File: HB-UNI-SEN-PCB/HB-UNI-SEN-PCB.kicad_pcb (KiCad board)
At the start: 2 copper layers, 44.4 x 30.5 mm, 18 parts, among them J0 BATT, J1 I2C_1, J2 I2C_2, J3 A0, J4 A1, J5 A2, J6 A3, J7 PROG, SW1 CONFIG_BUTTON, U1 ArduinoProMini, U2 CC1101

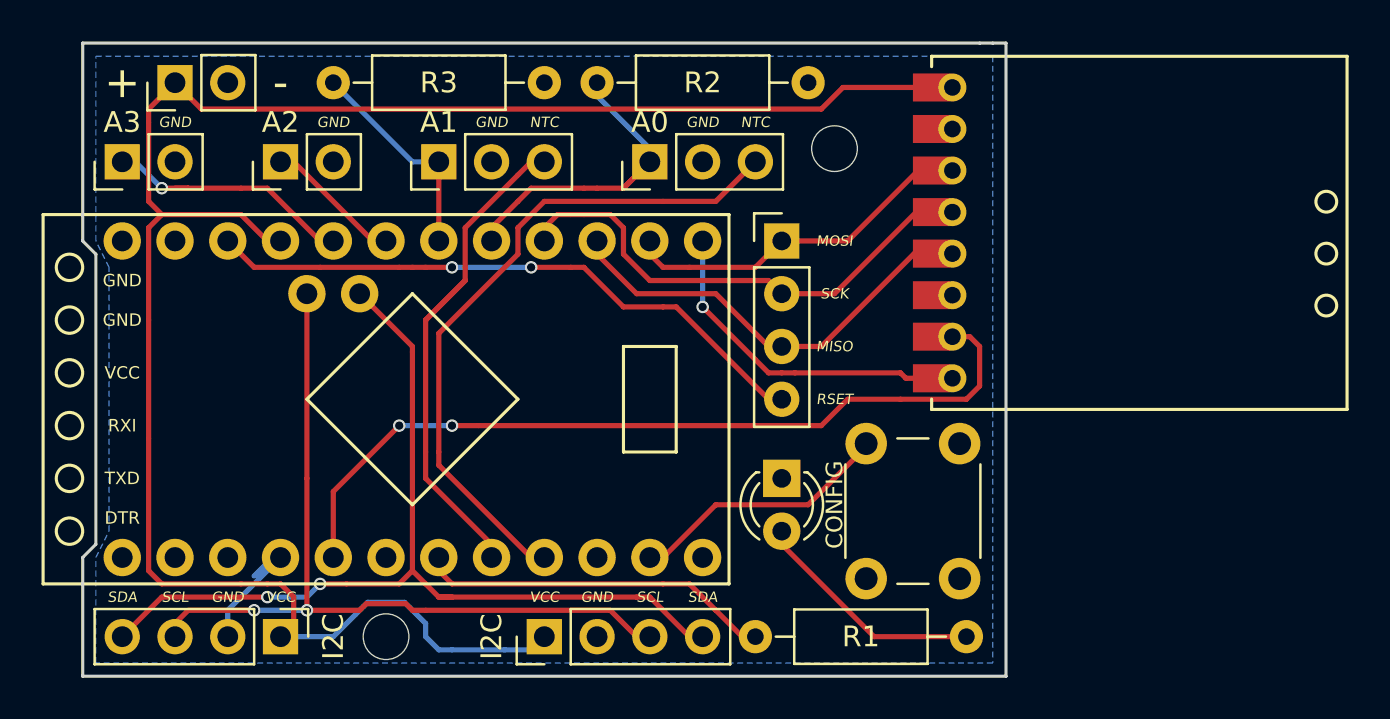
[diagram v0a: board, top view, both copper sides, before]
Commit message: Updated to v1.5: - Added raw power input - Moved two resistors and some jumpers - Rerouted some tracks
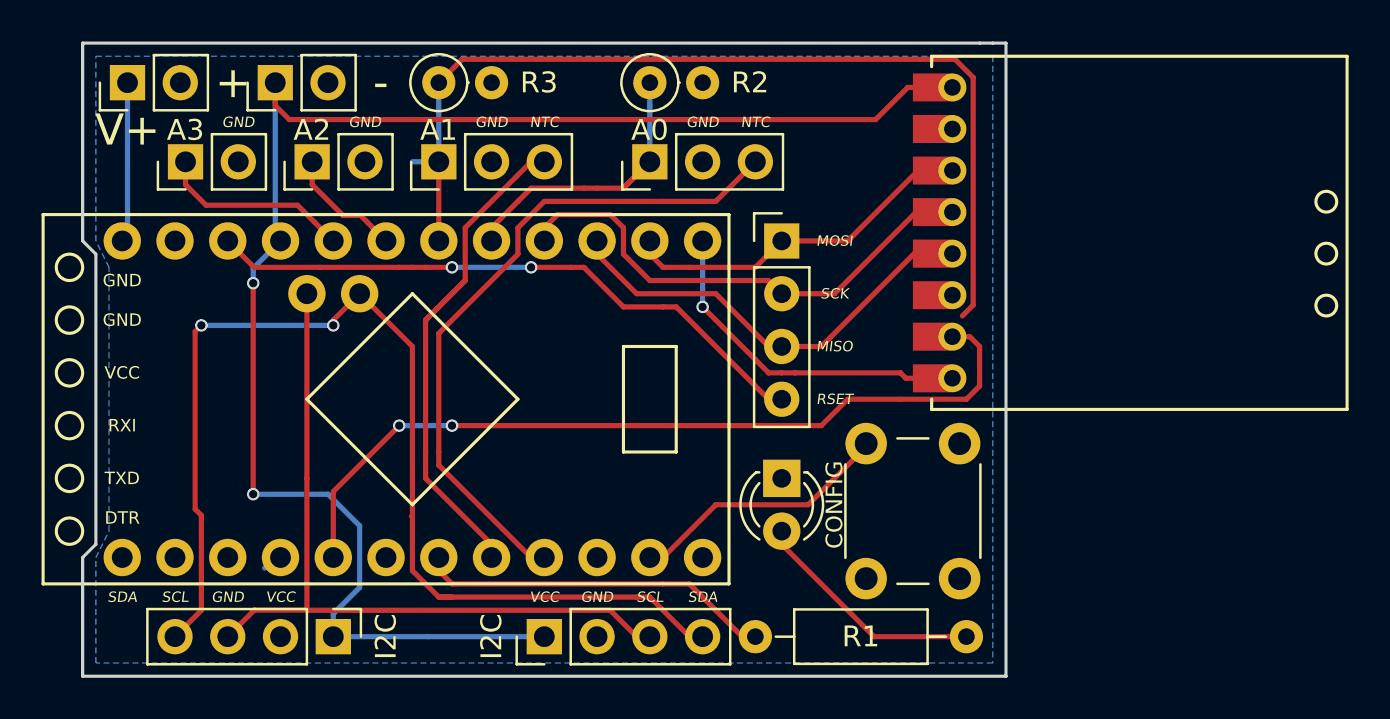
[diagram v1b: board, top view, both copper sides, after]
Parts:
- removed G***: LOGO, Homebrew:CC-BY-ND-SA
- removed REF** (x2): MountingHole_2.2mm_M2, Mounting_Holes:MountingHole_2.2mm_M2
- added JR1: RAW, Connector_PinHeader_2.54mm:PinHeader_1x02_P2.54mm_Vertical, F.Cu at (103.1, 49.5)
- R2, R3: footprint Resistors_THT:R_Axial_DIN0207_L6.3mm_D2.5mm_P10.16mm_Horizontal -> Resistor_THT:R_Axial_DIN0207_L6.3mm_D2.5mm_P2.54mm_Vertical
- moved R3 5.08 mm to (118.1, 49.5)
- moved J0 4.83 mm to (110.2, 49.5)
- moved J6 3.05 mm to (105.9, 53.3)
- moved J1 2.54 mm to (113.0, 76.2)
- moved R2 2.54 mm to (128.3, 49.5)
- moved J5 1.52 mm to (112.0, 53.3)
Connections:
- U1 pad 12: Net-(U1-Pad12) -> +12V
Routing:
- net /A1: track 11.1 -> 47.8 mm
- net +3V3: track 93.8 -> 77.9 mm, vias 0 -> 2
- net /SDA: track 46.5 -> 56.1 mm
- net +12V: track 0.00 -> 7.73 mm
- net GND: track 9.01 -> 2.35 mm
- net /SCL: track 39.8 -> 36.6 mm, vias 2 -> 0
- net /A3: track 13.0 -> 9.97 mm, vias 1 -> 0
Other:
- board text added: "(c) Alexander Reinert (c) Herr Frei"
- board text added: "V+"
- board text added: "Version 1.5 - 02/2019"
- board text removed: "(c) Alexander Reinert"
- board text removed: "Version 1.4 - 08/2018"

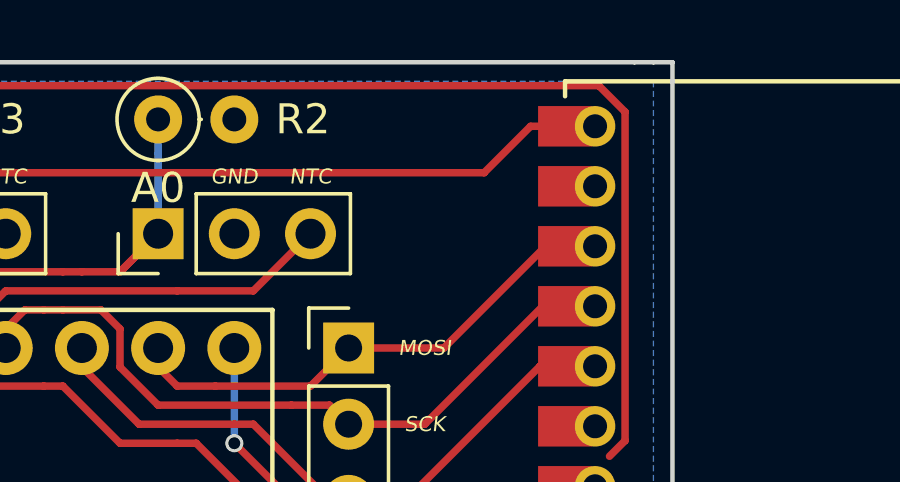
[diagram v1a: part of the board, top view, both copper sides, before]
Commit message: Added missing capacitor at CC1101
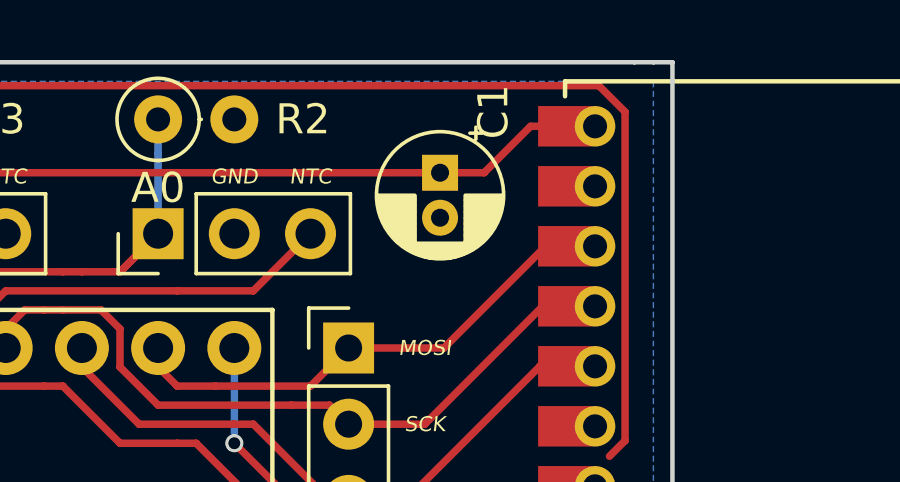
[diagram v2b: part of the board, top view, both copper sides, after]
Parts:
- added C1: 10uF, Capacitor_THT:CP_Radial_D4.0mm_P1.50mm, F.Cu at (137.7, 51.3)
